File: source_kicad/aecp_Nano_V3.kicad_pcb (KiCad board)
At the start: 2 copper layers, 86.5 x 88 mm, 30 parts, among them P1 CONN_IGBT, P10 FIX, P11 FIX, P12 CONN_SEL2, P13 CONN_DEP2, P14 MP3V5050, P15 FIX, P16 FIX, P17 FIX, P18 FIX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

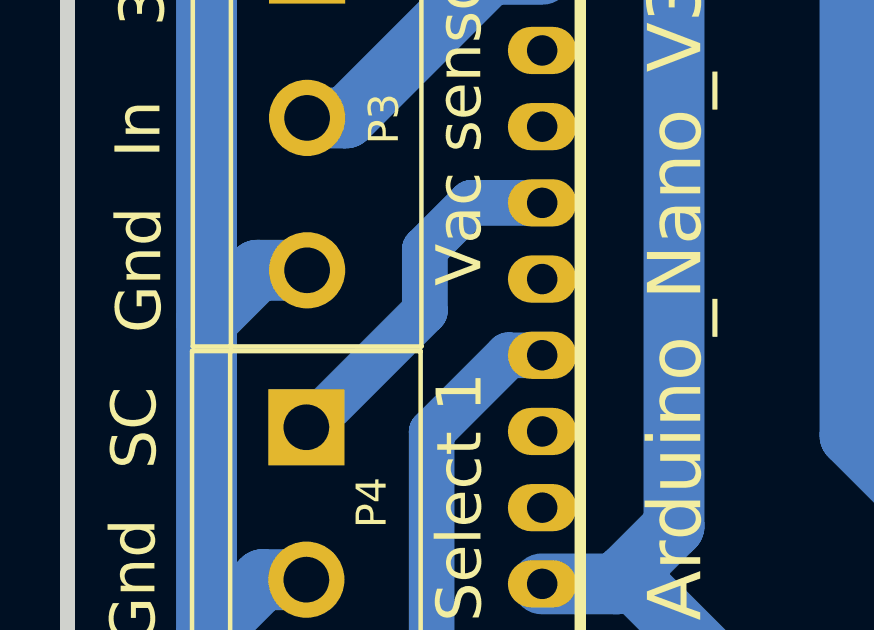
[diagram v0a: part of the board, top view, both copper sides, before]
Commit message: Bug corrected in the PCB
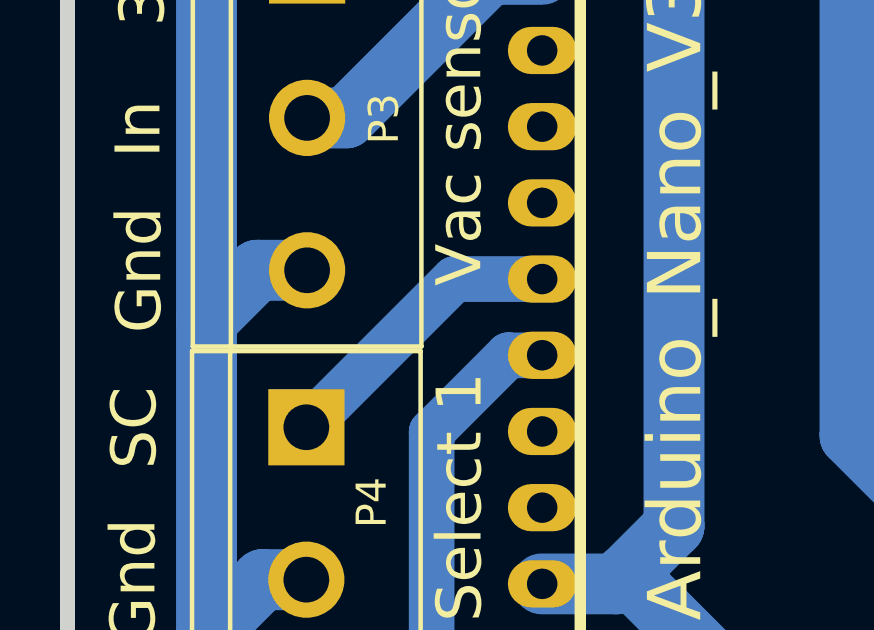
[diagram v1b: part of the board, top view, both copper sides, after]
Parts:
- G2: value Panhard24CT -> 24CT
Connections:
- U1 pad 7: Net-(P4-Pad1) -> Net-(U1-Pad7)
- U1 pad 8: Net-(U1-Pad8) -> Net-(P4-Pad1)
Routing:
- net Net-(P4-Pad1): track 12.2 -> 9.98 mm
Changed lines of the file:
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@@
     (links 34)
     (no_connects 2)
-    (area 61.249999 27.249999 163.781212 121.556881)
+    (area 61.249999 27.249999 148.249001 115.750001)
     (thickness 1.6)
     (drawings 62)
-    (tracks 136)
+    (tracks 134)
     (zones 0)
     (modules 30)
@@
   )
   (setup
-    (last_trace_width 0.25)
+    (last_trace_width 1.524)
     (user_trace_width 0.508)
     (user_trace_width 0.762)
@@
   (net 41 "Net-(C2-Pad2)")
   (net 42 "Net-(C3-Pad2)")
-  (net 43 "Net-(U1-Pad8)")
-  (net 44 "Net-(U1-Pad10)")
-  (net 45 "Net-(P1-Pad2)")
-  (net 46 "Net-(P5-Pad2)")
-  (net 47 "Net-(P15-Pad1)")
-  (net 48 "Net-(P16-Pad1)")
-  (net 49 "Net-(P17-Pad1)")
-  (net 50 "Net-(P18-Pad1)")
+  (net 43 "Net-(U1-Pad10)")
+  (net 44 "Net-(P1-Pad2)")
+  (net 45 "Net-(P5-Pad2)")
+  (net 46 "Net-(P15-Pad1)")
+  (net 47 "Net-(P16-Pad1)")
+  (net 48 "Net-(P17-Pad1)")
+  (net 49 "Net-(P18-Pad1)")
+  (net 50 "Net-(U1-Pad7)")
   (net_class Default "Ceci est la Netclass par défaut"
     (clearance 0.2)
@@
     (add_net "Net-(U1-Pad5)")
     (add_net "Net-(U1-Pad6)")
-    (add_net "Net-(U1-Pad8)")
+    (add_net "Net-(U1-Pad7)")
   )
   (module Connect:bornier2 (layer F.Cu)
@@
       (net 34 "Net-(U1-Pad6)"))
     (pad 7 thru_hole oval (at -3.81 7.62 270) (size 1.5748 2.286) (drill 1.016) (layers *.Cu *.Mask F.SilkS)
-      (net 20 "Net-(P4-Pad1)"))
+      (net 50 "Net-(U1-Pad7)"))
     (pad 8 thru_hole oval (at -1.27 7.62 270) (size 1.5748 2.286) (drill 1.016) (layers *.Cu *.Mask F.SilkS)
-      (net 43 "Net-(U1-Pad8)"))
+      (net 20 "Net-(P4-Pad1)"))
     (pad 9 thru_hole oval (at 1.27 7.62 270) (size 1.5748 2.286) (drill 1.016) (layers *.Cu *.Mask F.SilkS)
       (net 35 "Net-(P12-Pad1)"))
     (pad 10 thru_hole oval (at 3.81 7.62 270) (size 1.5748 2.286) (drill 1.016) (layers *.Cu *.Mask F.SilkS)
-      (net 44 "Net-(U1-Pad10)"))
+      (net 43 "Net-(U1-Pad10)"))
     (pad 11 thru_hole oval (at 6.35 7.62 270) (size 1.5748 2.286) (drill 1.016) (layers *.Cu *.Mask F.SilkS)
       (net 3 "Net-(U1-Pad11)"))
@@
       (net 9 GND))
     (pad 2 thru_hole circle (at 2.54 0 270) (size 2.54 2.54) (drill 1.524) (layers *.Cu *.Mask F.SilkS)
-      (net 46 "Net-(P5-Pad2)"))
+      (net 45 "Net-(P5-Pad2)"))
     (model walter/conn_screw/mors_2p.wrl
       (at (xyz 0 0 0))
@@
     (fp_line (start 0 -3.048) (end 5.334 -3.048) (layer F.SilkS) (width 0.15))
     (pad 2 thru_hole oval (at 0 0) (size 2.49936 1.50114) (drill 1.016) (layers *.Cu *.Mask F.SilkS)
-      (net 45 "Net-(P1-Pad2)"))
+      (net 44 "Net-(P1-Pad2)"))
     (pad 1 thru_hole oval (at -2.54 0) (size 2.49936 1.50114) (drill 1.016) (layers *.Cu *.Mask F.SilkS)
       (net 23 "Net-(Q1-Pad1)"))
@@
       (net 9 GND))
     (pad 1 thru_hole oval (at -2.54 0 90) (size 3.50012 1.69926) (drill 1.016) (layers *.Cu *.Mask F.SilkS)
-      (net 46 "Net-(P5-Pad2)"))
+      (net 45 "Net-(P5-Pad2)"))
     (pad 3 thru_hole oval (at 2.54 0 90) (size 3.50012 1.69926) (drill 1.016) (layers *.Cu *.Mask F.SilkS)
       (net 22 +5V))
@@
       (net 17 "Net-(P1-Pad1)"))
     (pad 2 thru_hole circle (at 2.54 0 270) (size 2.54 2.54) (drill 1.524) (layers *.Cu *.Mask F.SilkS)
-      (net 45 "Net-(P1-Pad2)"))
+      (net 44 "Net-(P1-Pad2)"))
     (model walter/conn_screw/mors_2p.wrl
       (at (xyz 0 0 0))
@@
       (effects (font (thickness 0.3)) (justify mirror))
     )
-    (fp_text value Panhard24CT (at 0.75 0 270) (layer B.SilkS) hide
+    (fp_text value 24CT (at 0.75 0 270) (layer B.SilkS) hide
       (effects (font (thickness 0.3)) (justify mirror))
     )
@@
     (fp_circle (center 0 0) (end 0 -2.286) (layer F.SilkS) (width 0.15))
     (pad 1 thru_hole circle (at 0 0) (size 4.064 4.064) (drill 3.048) (layers *.Cu *.Mask F.SilkS)
-      (net 47 "Net-(P15-Pad1)"))
+      (net 46 "Net-(P15-Pad1)"))
   )
   (module Connect:1pin (layer F.Cu)
@@
     (fp_circle (center 0 0) (end 0 -2.286) (layer F.SilkS) (width 0.15))
     (pad 1 thru_hole circle (at 0 0) (size 4.064 4.064) (drill 3.048) (layers *.Cu *.Mask F.SilkS)
-      (net 48 "Net-(P16-Pad1)"))
+      (net 47 "Net-(P16-Pad1)"))
   )
   (module Connect:1pin (layer F.Cu)
@@
     (fp_circle (center 0 0) (end 0 -2.286) (layer F.SilkS) (width 0.15))
     (pad 1 thru_hole circle (at 0 0) (size 4.064 4.064) (drill 3.048) (layers *.Cu *.Mask F.SilkS)
-      (net 49 "Net-(P17-Pad1)"))
+      (net 48 "Net-(P17-Pad1)"))
   )
   (module Connect:1pin (layer F.Cu)
@@
     (fp_circle (center 0 0) (end 0 -2.286) (layer F.SilkS) (width 0.15))
     (pad 1 thru_hole circle (at 0 0) (size 4.064 4.064) (drill 3.048) (layers *.Cu *.Mask F.SilkS)
-      (net 50 "Net-(P18-Pad1)"))
+      (net 49 "Net-(P18-Pad1)"))
   )
   (dimension 43.027967 (width 0.3) (layer Cmts.User)
@@
   (segment (start 75.57008 53.9623) (end 70.78218 58.7502) (width 2.032) (layer B.Cu) (net 19))
   (segment (start 77.29982 53.98516) (end 77.32268 53.9623) (width 1.016) (layer B.Cu) (net 19) (status 30))
+  (segment (start 77.32268 64.1223) (end 74.40168 64.1223) (width 1.524) (layer B.Cu) (net 20) (status 400000))
+  (segment (start 74.40168 64.1223) (end 69.46138 69.0626) (width 1.524) (layer B.Cu) (net 20) (status 800000))
   (segment (start 69.46138 69.0626) (end 69.53758 69.0626) (width 1.524) (layer B.Cu) (net 20))
-  (segment (start 69.53758 69.0626) (end 73.41108 65.1891) (width 1.524) (layer B.Cu) (net 20))
-  (segment (start 73.41108 65.1891) (end 73.41108 63.1317) (width 1.524) (layer B.Cu) (net 20))
-  (segment (start 73.41108 63.1317) (end 74.96048 61.5823) (width 1.524) (layer B.Cu) (net 20))
-  (segment (start 74.96048 61.5823) (end 77.32268 61.5823) (width 1.524) (layer B.Cu) (net 20))
   (segment (start 69.48678 38.227) (end 81.62798 38.227) (width 2.032) (layer B.Cu) (net 21))
   (segment (start 89.98458 71.7423) (end 92.56268 71.7423) (width 2.032) (layer B.Cu) (net 21))
@@
   (segment (start 141.1135 37.7152) (end 141.0589 37.7698) (width 1.016) (layer B.Cu) (net 42) (status 30))
   (segment (start 141.0843 37.7444) (end 141.0589 37.7698) (width 1.016) (layer B.Cu) (net 42) (status 30))
-  (segment (start 98.45548 53.58384) (end 102.91572 53.58384) (width 2.032) (layer B.Cu) (net 45))
-  (segment (start 75.29576 105.1052) (end 69.41058 105.1052) (width 2.032) (layer B.Cu) (net 45))
-  (segment (start 78.74 108.54944) (end 75.29576 105.1052) (width 2.032) (layer B.Cu) (net 45))
-  (segment (start 104.06888 108.54944) (end 78.74 108.54944) (width 2.032) (layer B.Cu) (net 45))
-  (segment (start 107.62996 104.98836) (end 104.06888 108.54944) (width 2.032) (layer B.Cu) (net 45))
-  (segment (start 107.62996 58.29808) (end 107.62996 104.98836) (width 2.032) (layer B.Cu) (net 45))
-  (segment (start 102.91572 53.58384) (end 107.62996 58.29808) (width 2.032) (layer B.Cu) (net 45))
-  (segment (start 69.42328 94.7674) (end 78.82128 94.7674) (width 2.032) (layer B.Cu) (net 46))
-  (segment (start 78.82128 94.7674) (end 82.40268 98.3488) (width 2.032) (layer B.Cu) (net 46))
-  (segment (start 82.37728 98.3234) (end 82.40268 98.3488) (width 1.524) (layer B.Cu) (net 46) (status 30))
+  (segment (start 98.45548 53.58384) (end 102.91572 53.58384) (width 2.032) (layer B.Cu) (net 44))
+  (segment (start 75.29576 105.1052) (end 69.41058 105.1052) (width 2.032) (layer B.Cu) (net 44))
+  (segment (start 78.74 108.54944) (end 75.29576 105.1052) (width 2.032) (layer B.Cu) (net 44))
+  (segment (start 104.06888 108.54944) (end 78.74 108.54944) (width 2.032) (layer B.Cu) (net 44))
+  (segment (start 107.62996 104.98836) (end 104.06888 108.54944) (width 2.032) (layer B.Cu) (net 44))
+  (segment (start 107.62996 58.29808) (end 107.62996 104.98836) (width 2.032) (layer B.Cu) (net 44))
+  (segment (start 102.91572 53.58384) (end 107.62996 58.29808) (width 2.032) (layer B.Cu) (net 44))
+  (segment (start 69.42328 94.7674) (end 78.82128 94.7674) (width 2.032) (layer B.Cu) (net 45))
+  (segment (start 78.82128 94.7674) (end 82.40268 98.3488) (width 2.032) (layer B.Cu) (net 45))
+  (segment (start 82.37728 98.3234) (end 82.40268 98.3488) (width 1.524) (layer B.Cu) (net 45) (status 30))
 )
